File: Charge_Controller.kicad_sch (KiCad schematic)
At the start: 156 parts, among them J1 SOLAR, J10 Conn_01x01_Female, J11 Conn_01x01_Female, J12 Conn_01x01_Female, J13 Conn_01x01_Female, J14 Conn_01x01_Female, J15 Conn_01x01_Female, J16 Conn_01x01_Female, J17 Conn_01x01_Female, J18 Conn_01x01_Female, J19 Conn_01x01_Female, J2 Conn_01x01_Female, J20 Conn_01x01_Female, J21 Conn_01x01_Female, J22 Conn_01x01_Female, J23 Conn_01x01_Female, J24 Conn_01x01_Female, J25 Conn_01x01_Female, J26 Conn_01x01_Female, J27 Conn_01x01_Female, J28 Conn_01x01_Female, J29 Conn_01x01_Female, J3 Conn_01x01_Female, J30 Conn_01x01_Female, J31 Conn_01x01_Female, J32 Conn_01x01_Female, J33 Conn_01x01_Female, J34 Conn_01x01_Female, J36 FAN, J38 I2C_CON, J4 Conn_01x01_Female, J5 Conn_01x01_Female, J6 Conn_01x01_Female, J7 Conn_01x01_Female, J8 BATT, J9 USB_OTG, Q1 CSD19505, Q2 CSD19505, Q3 CSD19505, Q4 Si2306, Q5 2N3904, Q6 2N3904, Q7 PMOS-100V-78A, Q8 PMOS-100V-78A, Q9 Si2306, SW1 RIGHT, SW2 LEFT, SW3 BACK, SW4 SELECT, U1 ACS712-30A, U10 ADS1015, U11 NUP4202, U12 PCF8574, U2 B1212, U3 AMS1117-5.0, U4 AMS1117-3.3, U5 XL7005A, U6 XL7005A, U7 IR2104, U8 ESP32-WROOM-32, U9 CH340C

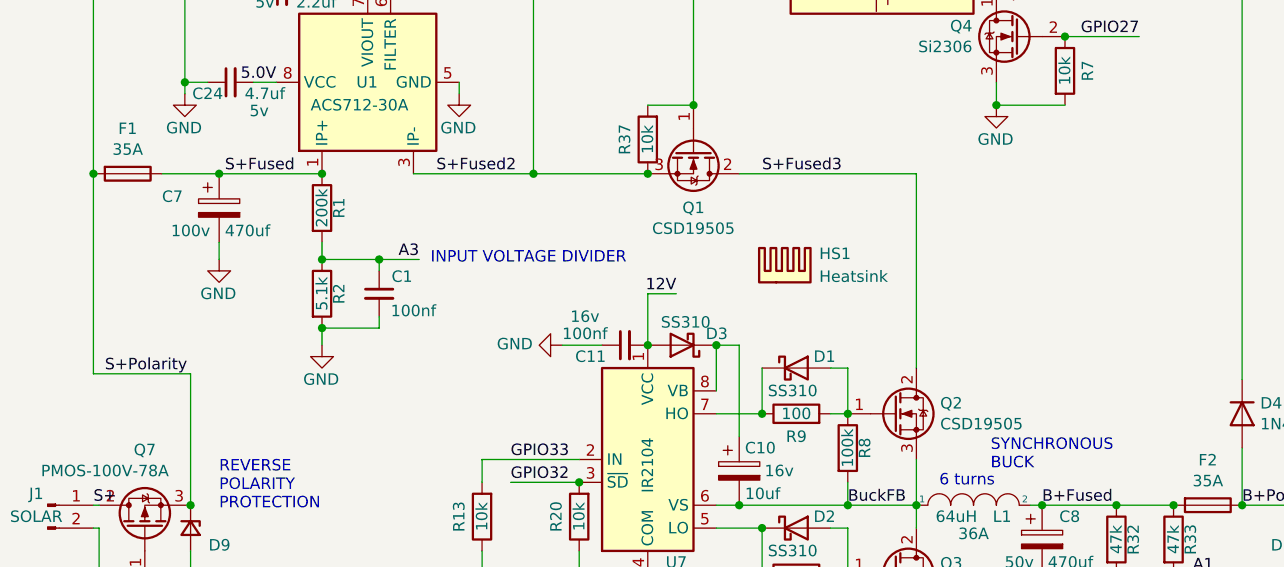
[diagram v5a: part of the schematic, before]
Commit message: Moved C7 to other side of current sensor, changed C7 and C8 from Axial to Radial, moved U3 slightly. https://github.com/jharvey/Charge_Controller/issues/2
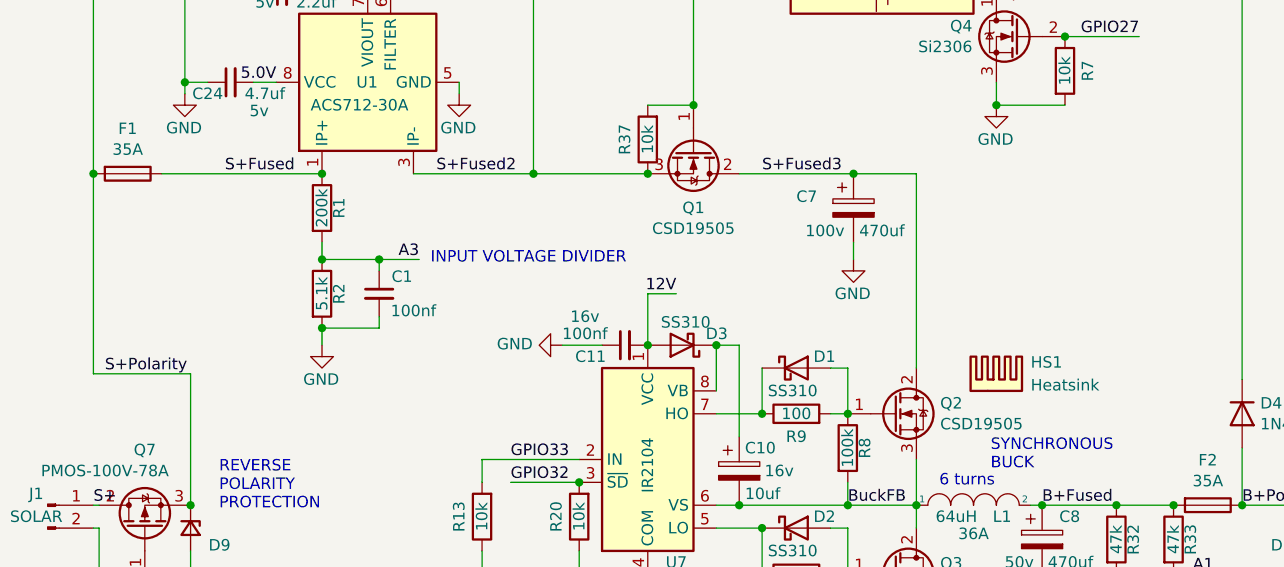
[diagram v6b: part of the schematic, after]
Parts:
- C7, C8: footprint Capacitor_THT:CP_Axial_L30.0mm_D18.0mm_P35.00mm_Horizontal -> Capacitor_THT:CP_Radial_D16.0mm_P7.50mm; Digikey 4100PHBK-ND -> (none); LCSC NA -> C513392
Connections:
- net S+Fused: no longer C7.1
- net S+Fused3: now also C7.1
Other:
- moved on the sheet: HS1
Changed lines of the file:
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@@
   (junction (at 42.545 55.88) (diameter 0) (color 0 0 0 0)
   )
-  (junction (at 36.195 115.57) (diameter 0) (color 0 0 0 0)
-  )
   (junction (at 100.33 55.88) (diameter 0) (color 0 0 0 0)
   )
@@
   (junction (at 127.635 47.625) (diameter 0) (color 0 0 0 0)
   )
+  (junction (at 106.68 115.57) (diameter 0) (color 0 0 0 0)
+  )
   (junction (at 333.375 64.135) (diameter 0) (color 0 0 0 0)
   )
@@
     (stroke (width 0) (type default) (color 0 0 0 0))
   )
-  (wire (pts (xy 36.195 123.19) (xy 36.195 125.095))
-    (stroke (width 0) (type default) (color 0 0 0 0))
-  )
   (wire (pts (xy 83.82 160.02) (xy 83.82 160.655))
     (stroke (width 0) (type default) (color 0 0 0 0))
@@
     (stroke (width 0) (type default) (color 0 0 0 0))
   )
-  (wire (pts (xy 36.195 115.57) (xy 47.625 115.57))
-    (stroke (width 0) (type default) (color 0 0 0 0))
-  )
   (wire (pts (xy 22.225 152.4) (xy 22.86 152.4))
     (stroke (width 0) (type default) (color 0 0 0 0))
@@
     (stroke (width 0) (type default) (color 0 0 0 0))
   )
+  (wire (pts (xy 106.68 123.19) (xy 106.68 125.095))
+    (stroke (width 0) (type default) (color 0 0 0 0))
+  )
   (wire (pts (xy 172.72 24.765) (xy 188.595 24.765))
     (stroke (width 0) (type default) (color 0 0 0 0))
@@
     (stroke (width 0) (type default) (color 0 0 0 0))
   )
-  (wire (pts (xy 93.98 115.57) (xy 113.665 115.57))
+  (wire (pts (xy 93.98 115.57) (xy 106.68 115.57))
     (stroke (width 0) (type default) (color 0 0 0 0))
   )
@@
     (stroke (width 0) (type default) (color 0 0 0 0))
   )
+  (wire (pts (xy 106.68 115.57) (xy 113.665 115.57))
+    (stroke (width 0) (type default) (color 0 0 0 0))
+  )
   (wire (pts (xy 120.015 47.625) (xy 127.635 47.625))
     (stroke (width 0) (type default) (color 0 0 0 0))
@@
     (stroke (width 0) (type default) (color 0 0 0 0))
   )
-  (wire (pts (xy 29.845 115.57) (xy 36.195 115.57))
+  (wire (pts (xy 29.845 115.57) (xy 47.625 115.57))
     (stroke (width 0) (type default) (color 0 0 0 0))
   )
@@
     (pin "2")
   )
-  (symbol (lib_id "Device:C_Polarized") (at 36.195 119.38 0) (unit 1)
-    (in_bom yes) (on_board yes)
-    (property "Reference" "C7" (id 0) (at 29.845 118.11 0)
-      (effects (font (size 1.27 1.27)) (justify left))
-    )
-    (property "Value" "470uf" (id 1) (at 36.83 121.92 0)
-      (effects (font (size 1.27 1.27)) (justify left))
-    )
-    (property "Footprint" "Capacitor_THT:CP_Axial_L30.0mm_D18.0mm_P35.00mm_Horizontal" (id 2) (at 37.1602 123.19 0)
-      (effects (font (size 1.27 1.27)) hide)
-    )
-    (property "Datasheet" "~" (id 3) (at 36.195 119.38 0)
-      (effects (font (size 1.27 1.27)) hide)
-    )
-    (property "Digikey" "4100PHBK-ND" (id 4) (at 36.195 119.38 0)
-      (effects (font (size 1.27 1.27)) hide)
-    )
-    (property "LCSC" "NA" (id 5) (at 36.195 119.38 0)
-      (effects (font (size 1.27 1.27)) hide)
-    )
-    (property "Field4" "100v" (id 6) (at 33.02 121.92 0))
-    (pin "1")
-    (pin "2")
-  )
-  (symbol (lib_id "power:GND") (at 36.195 125.095 0) (unit 1)
-    (in_bom yes) (on_board yes)
-    (property "Reference" "#PWR05" (id 0) (at 36.195 131.445 0)
-      (effects (font (size 1.27 1.27)) hide)
-    )
-    (property "Value" "GND" (id 1) (at 38.1 128.905 0)
-      (effects (font (size 1.27 1.27)) (justify right))
-    )
-    (property "Footprint" "" (id 2) (at 36.195 125.095 0)
-      (effects (font (size 1.27 1.27)) hide)
-    )
-    (property "Datasheet" "" (id 3) (at 36.195 125.095 0)
-      (effects (font (size 1.27 1.27)) hide)
-    )
-    (pin "1")
-  )
   (symbol (lib_id "power:GND") (at 74.295 134.62 270) (mirror x) (unit 1)
     (in_bom yes) (on_board yes)
@@
       (effects (font (size 1.27 1.27)) (justify left))
     )
-    (property "Footprint" "Capacitor_THT:CP_Axial_L30.0mm_D18.0mm_P35.00mm_Horizontal" (id 2) (at 128.6002 160.02 0)
+    (property "Footprint" "Capacitor_THT:CP_Radial_D16.0mm_P7.50mm" (id 2) (at 128.6002 160.02 0)
       (effects (font (size 1.27 1.27)) hide)
     )
@@
       (effects (font (size 1.27 1.27)) hide)
     )
-    (property "Digikey" "4100PHBK-ND" (id 4) (at 127.635 156.21 0)
+    (property "Digikey" "" (id 4) (at 127.635 156.21 0)
       (effects (font (size 1.27 1.27)) hide)
     )
-    (property "LCSC" "NA" (id 5) (at 127.635 156.21 0)
+    (property "LCSC" "C513392" (id 5) (at 127.635 156.21 0)
       (effects (font (size 1.27 1.27)) hide)
     )
@@
     (pin "2")
   )
+  (symbol (lib_id "Device:C_Polarized") (at 106.68 119.38 0) (unit 1)
+    (in_bom yes) (on_board yes)
+    (property "Reference" "C7" (id 0) (at 100.33 118.11 0)
+      (effects (font (size 1.27 1.27)) (justify left))
+    )
+    (property "Value" "470uf" (id 1) (at 107.315 121.92 0)
+      (effects (font (size 1.27 1.27)) (justify left))
+    )
+    (property "Footprint" "Capacitor_THT:CP_Radial_D16.0mm_P7.50mm" (id 2) (at 107.6452 123.19 0)
+      (effects (font (size 1.27 1.27)) hide)
+    )
+    (property "Datasheet" "~" (id 3) (at 106.68 119.38 0)
+      (effects (font (size 1.27 1.27)) hide)
+    )
+    (property "Digikey" "" (id 4) (at 106.68 119.38 0)
+      (effects (font (size 1.27 1.27)) hide)
+    )
+    (property "LCSC" "C513392" (id 5) (at 106.68 119.38 0)
+      (effects (font (size 1.27 1.27)) hide)
+    )
+    (property "Field4" "100v" (id 6) (at 103.505 121.92 0))
+    (pin "1")
+    (pin "2")
+  )
   (symbol (lib_id "Graphic:Logo_Open_Hardware_Small") (at 229.235 197.485 0) (unit 1)
     (in_bom yes) (on_board yes) (fields_autoplaced)
@@
     (pin "2")
   )
-  (symbol (lib_id "Mechanical:Heatsink") (at 99.06 127.635 0) (unit 1)
+  (symbol (lib_id "Mechanical:Heatsink") (at 122.555 139.7 0) (unit 1)
     (in_bom yes) (on_board yes) (fields_autoplaced)
-    (property "Reference" "HS1" (id 0) (at 102.87 124.4599 0)
+    (property "Reference" "HS1" (id 0) (at 126.365 136.5249 0)
       (effects (font (size 1.27 1.27)) (justify left))
     )
-    (property "Value" "Heatsink" (id 1) (at 102.87 126.9999 0)
+    (property "Value" "Heatsink" (id 1) (at 126.365 139.0649 0)
       (effects (font (size 1.27 1.27)) (justify left))
     )
-    (property "Footprint" "Heatsink:Heatsink_Stonecold_HS-132_32x14mm_2xFixation1.5mm" (id 2) (at 99.3648 127.635 0)
+    (property "Footprint" "Heatsink:Heatsink_Stonecold_HS-132_32x14mm_2xFixation1.5mm" (id 2) (at 122.8598 139.7 0)
       (effects (font (size 1.27 1.27)) hide)
     )
-    (property "Datasheet" "~" (id 3) (at 99.3648 127.635 0)
+    (property "Datasheet" "~" (id 3) (at 122.8598 139.7 0)
       (effects (font (size 1.27 1.27)) hide)
     )
-    (property "Digikey" "AE10798-ND" (id 4) (at 99.06 127.635 0)
+    (property "Digikey" "AE10798-ND" (id 4) (at 122.555 139.7 0)
       (effects (font (size 1.27 1.27)) hide)
     )
-    (property "LCSC" "NA" (id 5) (at 99.06 127.635 0)
+    (property "LCSC" "NA" (id 5) (at 122.555 139.7 0)
       (effects (font (size 1.27 1.27)) hide)
     )
@@
     (pin "1")
   )
+  (symbol (lib_id "power:GND") (at 106.68 125.095 0) (unit 1)
+    (in_bom yes) (on_board yes)
+    (property "Reference" "#PWR0101" (id 0) (at 106.68 131.445 0)
+      (effects (font (size 1.27 1.27)) hide)
+    )
+    (property "Value" "GND" (id 1) (at 108.585 128.905 0)
+      (effects (font (size 1.27 1.27)) (justify right))
+    )
+    (property "Footprint" "" (id 2) (at 106.68 125.095 0)
+      (effects (font (size 1.27 1.27)) hide)
+    )
+    (property "Datasheet" "" (id 3) (at 106.68 125.095 0)
+      (effects (font (size 1.27 1.27)) hide)
+    )
+    (pin "1")
+  )
   (symbol (lib_id "power:GND") (at 222.885 190.5 0) (unit 1)
     (in_bom yes) (on_board yes)
@@
       (reference "#PWR04") (unit 1) (value "GND") (footprint "")
     )
-    (path "/00000000-0000-0000-0000-00006353be9b"
-      (reference "#PWR05") (unit 1) (value "GND") (footprint "")
-    )
     (path "/00000000-0000-0000-0000-0000634f9b21"
       (reference "#PWR06") (unit 1) (value "GND") (footprint "")
@@
       (reference "#PWR048") (unit 1) (value "GND") (footprint "")
     )
+    (path "/e15e8d88-232f-4132-bfe4-01915996ef56"
+      (reference "#PWR0101") (unit 1) (value "GND") (footprint "")
+    )
     (path "/00000000-0000-0000-0000-0000634fa01d"
       (reference "C1") (unit 1) (value "100nf") (footprint "Capacitor_SMD:C_0805_2012Metric")
@@
       (reference "C6") (unit 1) (value "4.7uf") (footprint "Capacitor_SMD:C_0805_2012Metric")
     )
-    (path "/00000000-0000-0000-0000-00006353b3ec"
-      (reference "C7") (unit 1) (value "470uf") (footprint "Capacitor_THT:CP_Axial_L30.0mm_D18.0mm_P35.00mm_Horizontal")
+    (path "/53543877-af6f-4dc0-8bd9-c8793a35f681"
+      (reference "C7") (unit 1) (value "470uf") (footprint "Capacitor_THT:CP_Radial_D16.0mm_P7.50mm")
     )
     (path "/00000000-0000-0000-0000-0000636b1a52"
-      (reference "C8") (unit 1) (value "470uf") (footprint "Capacitor_THT:CP_Axial_L30.0mm_D18.0mm_P35.00mm_Horizontal")
+      (reference "C8") (unit 1) (value "470uf") (footprint "Capacitor_THT:CP_Radial_D16.0mm_P7.50mm")
     )
     (path "/00000000-0000-0000-0000-0000633468f8"

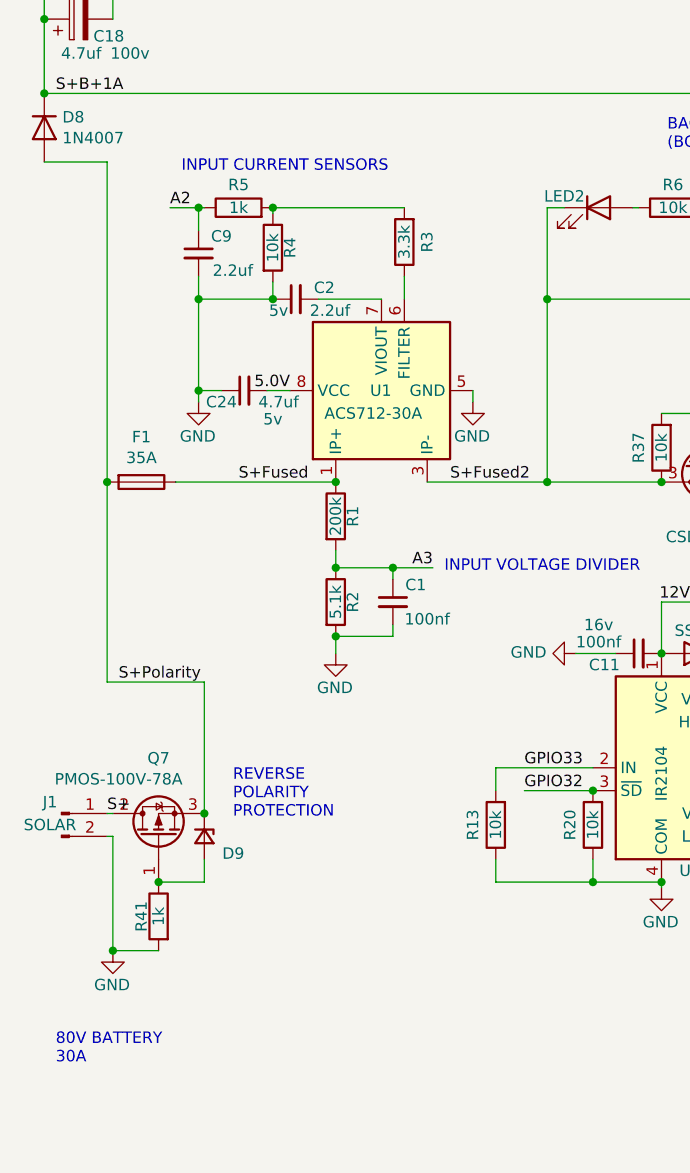
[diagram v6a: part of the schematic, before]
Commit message: Added D11, D12 and D13 for input surge protection. https://github.com/jharvey/Charge_Controller/issues/3
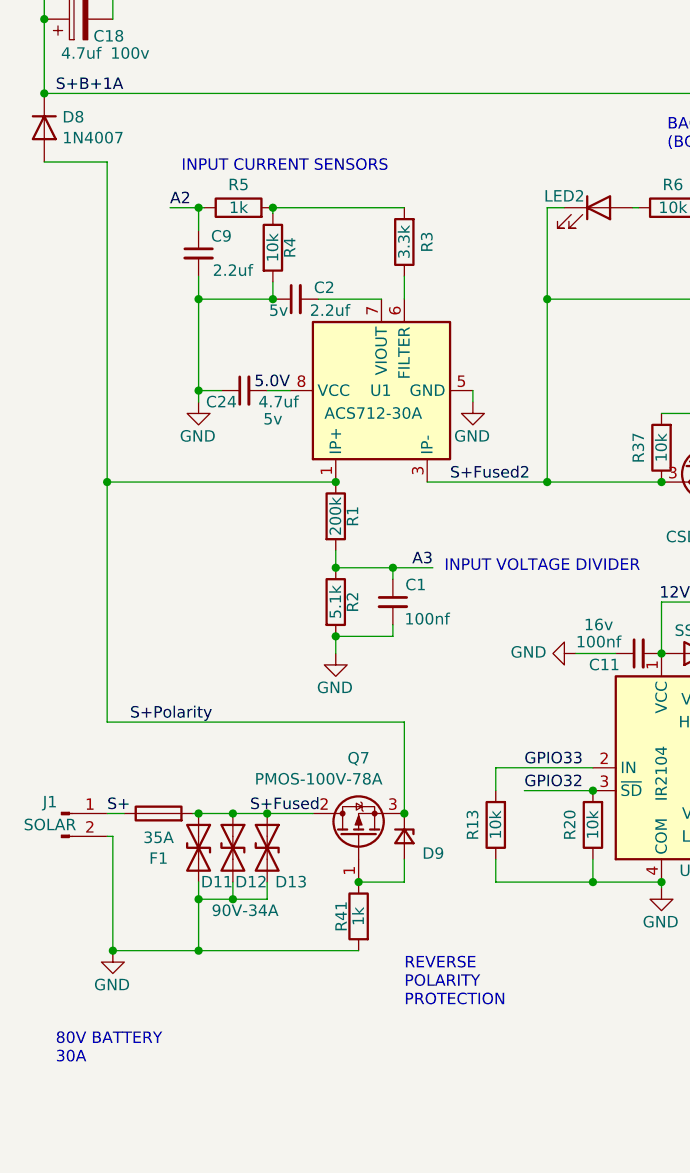
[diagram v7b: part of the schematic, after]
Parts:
- added D11: 90V-34A, Diode_SMD:D_SMC-RM10_Universal_Handsoldering, symbol Device:D_TVS
- added D12, D13: 120V-26A, Diode_SMD:D_SMC-RM10_Universal_Handsoldering, symbol Device:D_TVS
- D10, D9: footprint Diode_SMD:D_MiniMELF_Handsoldering -> Diode_SMD:D_MiniMELF
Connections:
- net GND: now also D11.2 (A2), D12.2 (A2), D13.2 (A2)
- net S+: now also F1.1; no longer Q7.2 (D)
- net S+Fused: now also F1.2, Q7.2 (D), D11.1 (A1), D12.1 (A1), D13.1 (A1); no longer F1.1, R1.1, U1.1 (IP+), U1.2 (IP+)
- net S+Polarity: now also R1.1, U1.1 (IP+), U1.2 (IP+); no longer F1.2
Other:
- moved on the sheet: D9, Q7, R41

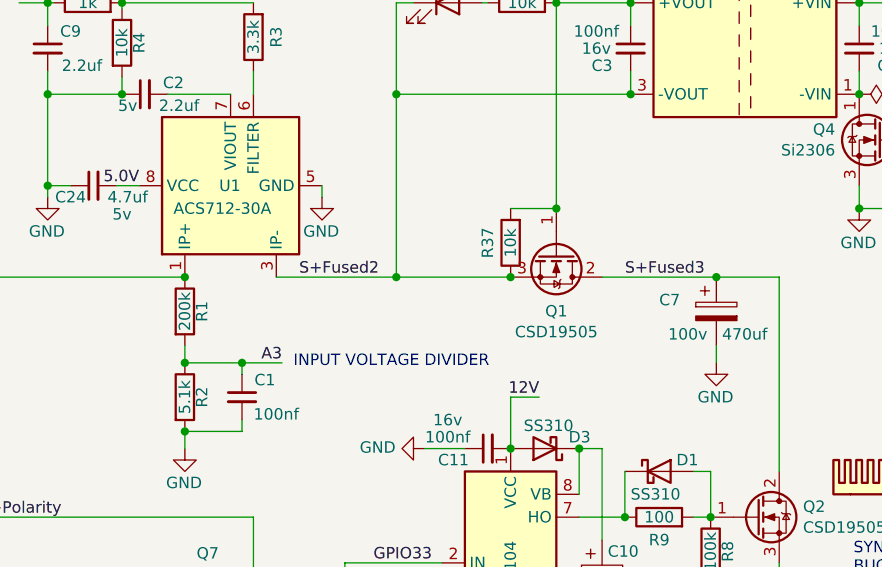
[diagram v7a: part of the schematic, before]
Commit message: Changed the hall sensor and added some notes.
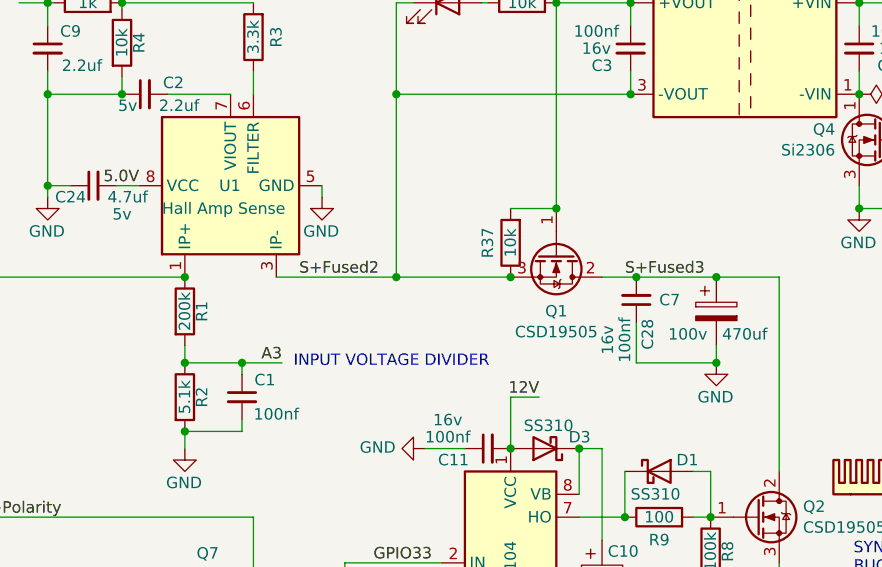
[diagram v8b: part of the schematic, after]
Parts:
- added C28: 100nf, Capacitor_SMD:C_0805_2012Metric, symbol Device:C_Small
- U1: value ACS712-30A -> Hall Amp Sense; LCSC C9932 -> C2930869
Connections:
- net GND: now also C28.1
- net S+Fused3: now also C28.2
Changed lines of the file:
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@@
   (junction (at 332.105 50.8) (diameter 0) (color 0 0 0 0)
   )
+  (junction (at 97.79 115.57) (diameter 0) (color 0 0 0 0)
+  )
   (junction (at 76.2 160.02) (diameter 0) (color 0 0 0 0)
   )
@@
   (junction (at 328.295 134.62) (diameter 0) (color 0 0 0 0)
   )
+  (junction (at 106.68 125.095) (diameter 0) (color 0 0 0 0)
+  )
   (junction (at 127.635 167.64) (diameter 0) (color 0 0 0 0)
   )
@@
     (stroke (width 0) (type default) (color 0 0 0 0))
   )
+  (wire (pts (xy 97.79 120.65) (xy 97.79 125.095))
+    (stroke (width 0) (type default) (color 0 0 0 0))
+  )
   (wire (pts (xy 332.105 38.1) (xy 332.105 36.83))
     (stroke (width 0) (type default) (color 0 0 0 0))
@@
     (stroke (width 0) (type default) (color 0 0 0 0))
   )
-  (wire (pts (xy 93.98 115.57) (xy 106.68 115.57))
+  (wire (pts (xy 93.98 115.57) (xy 97.79 115.57))
     (stroke (width 0) (type default) (color 0 0 0 0))
   )
@@
     (stroke (width 0) (type default) (color 0 0 0 0))
   )
+  (wire (pts (xy 97.79 125.095) (xy 106.68 125.095))
+    (stroke (width 0) (type default) (color 0 0 0 0))
+  )
   (wire (pts (xy 304.165 90.805) (xy 304.165 86.995))
     (stroke (width 0) (type default) (color 0 0 0 0))
@@
     (stroke (width 0) (type default) (color 0 0 0 0))
   )
+  (wire (pts (xy 97.79 115.57) (xy 106.68 115.57))
+    (stroke (width 0) (type default) (color 0 0 0 0))
+  )
   (wire (pts (xy 146.685 40.005) (xy 146.685 53.34))
     (stroke (width 0) (type default) (color 0 0 0 0))
@@
       (effects (font (size 1.27 1.27)) (justify right))
     )
-    (property "Value" "ACS712-30A" (id 1) (at 46.355 107.95 90)
+    (property "Value" "Hall Amp Sense" (id 1) (at 45.085 107.95 90)
       (effects (font (size 1.27 1.27)) (justify right))
     )
@@
       (effects (font (size 1.27 1.27)) hide)
     )
-    (property "LCSC" "C9932" (id 4) (at 52.705 105.41 0)
+    (property "LCSC" "C2930869" (id 4) (at 52.705 105.41 0)
       (effects (font (size 1.27 1.27)) hide)
     )
@@
     (pin "2")
   )
+  (symbol (lib_id "Device:C_Small") (at 97.79 118.11 0) (mirror x) (unit 1)
+    (in_bom yes) (on_board yes)
+    (property "Reference" "C28" (id 0) (at 99.06 121.92 90))
+    (property "Value" "100nf" (id 1) (at 96.52 122.555 90))
+    (property "Footprint" "Capacitor_SMD:C_0805_2012Metric" (id 2) (at 97.79 118.11 0)
+      (effects (font (size 1.27 1.27)) hide)
+    )
+    (property "Datasheet" "~" (id 3) (at 97.79 118.11 0)
+      (effects (font (size 1.27 1.27)) hide)
+    )
+    (property "Field4" "16v" (id 4) (at 94.615 122.555 90))
+    (property "LCSC" "C28233" (id 5) (at 97.79 118.11 0)
+      (effects (font (size 1.27 1.27)) hide)
+    )
+    (pin "1")
+    (pin "2")
+  )
   (symbol (lib_id "Graphic:Logo_Open_Hardware_Small") (at 229.235 197.485 0) (unit 1)
     (in_bom yes) (on_board yes) (fields_autoplaced)
@@
       (reference "C27") (unit 1) (value "100nf") (footprint "Capacitor_SMD:C_0805_2012Metric")
     )
+    (path "/5a8c586c-6ea7-4fc7-bf67-8bdffc83126c"
+      (reference "C28") (unit 1) (value "100nf") (footprint "Capacitor_SMD:C_0805_2012Metric")
+    )
     (path "/00000000-0000-0000-0000-0000635c8134"
       (reference "D1") (unit 1) (value "SS310") (footprint "Diode_SMD:D_SMA")
@@
     )
     (path "/00000000-0000-0000-0000-000063287365"
-      (reference "U1") (unit 1) (value "ACS712-30A") (footprint "Package_SO:SOIC-8_3.9x4.9mm_P1.27mm")
+      (reference "U1") (unit 1) (value "Hall Amp Sense") (footprint "Package_SO:SOIC-8_3.9x4.9mm_P1.27mm")
     )
     (path "/00000000-0000-0000-0000-00006317bc88"
